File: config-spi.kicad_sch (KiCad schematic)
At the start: 35 parts, among them J3001 PinHeader_2x7_P2mm_SMD_Shroud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, Q3001 BSS138PW, Q3002 BSS138PW, Q3003 BSS138PW, SW3001 SW_KMR211NGLFS_SMD, SW3002 CVS-03B, U3001 S25FL128SAGNFI000, U3002 XC7K160T-FFG676, U3003 TPD4E05U06QDQARQ1

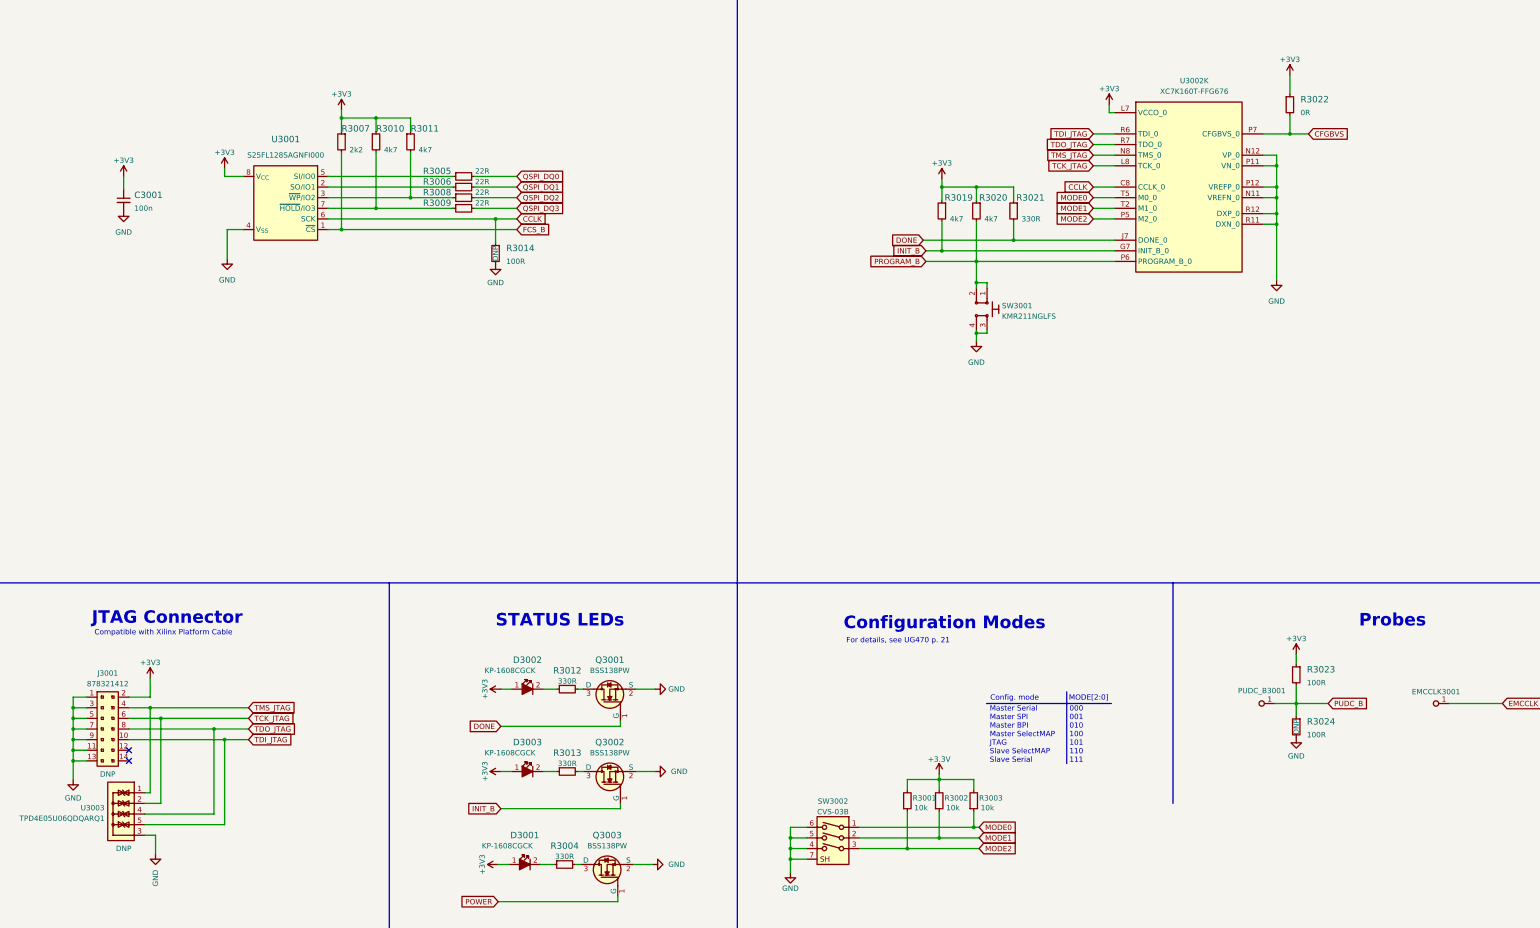
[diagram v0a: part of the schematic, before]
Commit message: Re-annotate schematic
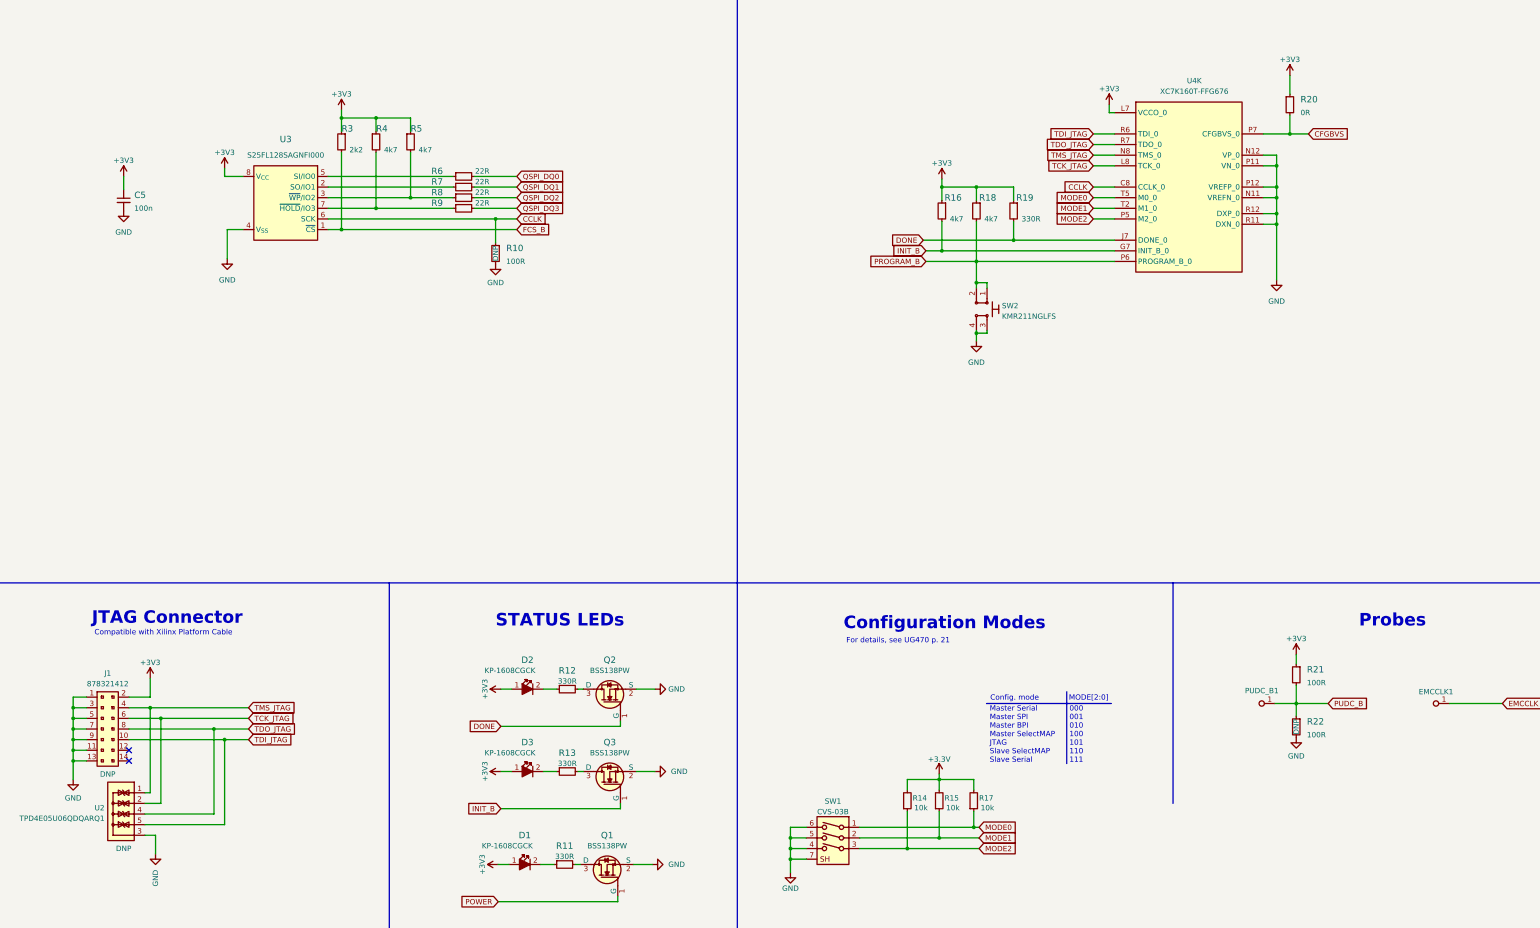
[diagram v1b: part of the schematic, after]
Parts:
- renumbered C3001 to C5, D3001 to D1, D3002 to D2, D3003 to D3, EMCCLK3001 to EMCCLK1, J3001 to J1, PUDC_B3001 to PUDC_B1, Q3003 to Q1, Q3001 to Q2, Q3002 to Q3, R3014 to R10, R3004 to R11, R3012 to R12, R3013 to R13, R3001 to R14, R3002 to R15, R3019 to R16, R3003 to R17, R3020 to R18, R3021 to R19, R3022 to R20, R3023 to R21, R3024 to R22, R3007 to R3, R3010 to R4, R3011 to R5, R3005 to R6, R3006 to R7, R3008 to R8, R3009 to R9, SW3002 to SW1, SW3001 to SW2, U3003 to U2, U3001 to U3, U3002 to U4

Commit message: Add local libraries
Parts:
- EMCCLK1, PUDC_B1: footprint antmicro-footprints:TP_SMD_1mm -> sodimm-ddr5-tester-footprints:TP_SMD_1mm; symbol antmicroTestPoints:TP_1mm_SMD -> sodimm-ddr5-tester:TP_1mm_SMD
- U2: footprint antmicro-footprints:USON-10_2.5x1mm_P0.5mm -> sodimm-ddr5-tester-footprints:USON-10_2.5x1mm_P0.5mm; symbol antmicroTVSDiodes:TPD4E05U06QDQARQ1 -> sodimm-ddr5-tester:TPD4E05U06QDQARQ1

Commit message: Connect DDR hierarchical labels. Define and connect JTAG, RGMII, TDMS, UART, and SDIO buses. Reorganize schematic blocks between sheets
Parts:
- removed EMCCLK1, PUDC_B1: TP_1mm_SMD, sodimm-ddr5-tester-footprints:TP_SMD_1mm, symbol sodimm-ddr5-tester:TP_1mm_SMD
- removed R21, R22: R_100R_0402, sodimm-ddr5-tester-footprints:R_0402_1005Metric, symbol sodimm-ddr5-tester:R_100R_0402
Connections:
- net TCK_JTAG renamed JTAG.TCK
- net TDI_JTAG renamed JTAG.TDI
- net TDO_JTAG renamed JTAG.TDO
- net TMS_JTAG renamed JTAG.TMS
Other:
- note removed: "Probes"
- moved on the sheet: C5, J1, R14, R15, R17, R20, U2
